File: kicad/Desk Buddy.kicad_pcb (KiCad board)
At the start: 2 copper layers, 62 parts, among them J1 USB_C_Receptacle_USB2.0_16P, J10 EXP_I2C1_2, J11 EXT_LED, J12 Conn_01x06, J13 Motor, J14 Conn_01x02, J15 TTP_1, J16 TTP_2, J17 UART, J2 LiPo, J3 GPIO48, J4 LCD_A, J5 LCD_B, J6 ToF, J7 AHT+BMP, J8 MPU6050, J9 EXP_I2C1_1, Q1 AO3400A, Q2 AO3400A, SW1 Push_EN, SW2 Push_BOOT, SW3 Switch_POWER, U1 USBLC6-2SC6, U2 BQ24075RGT, U3 AP2112K-3.3, U4 ESP32-S3-WROOM-1

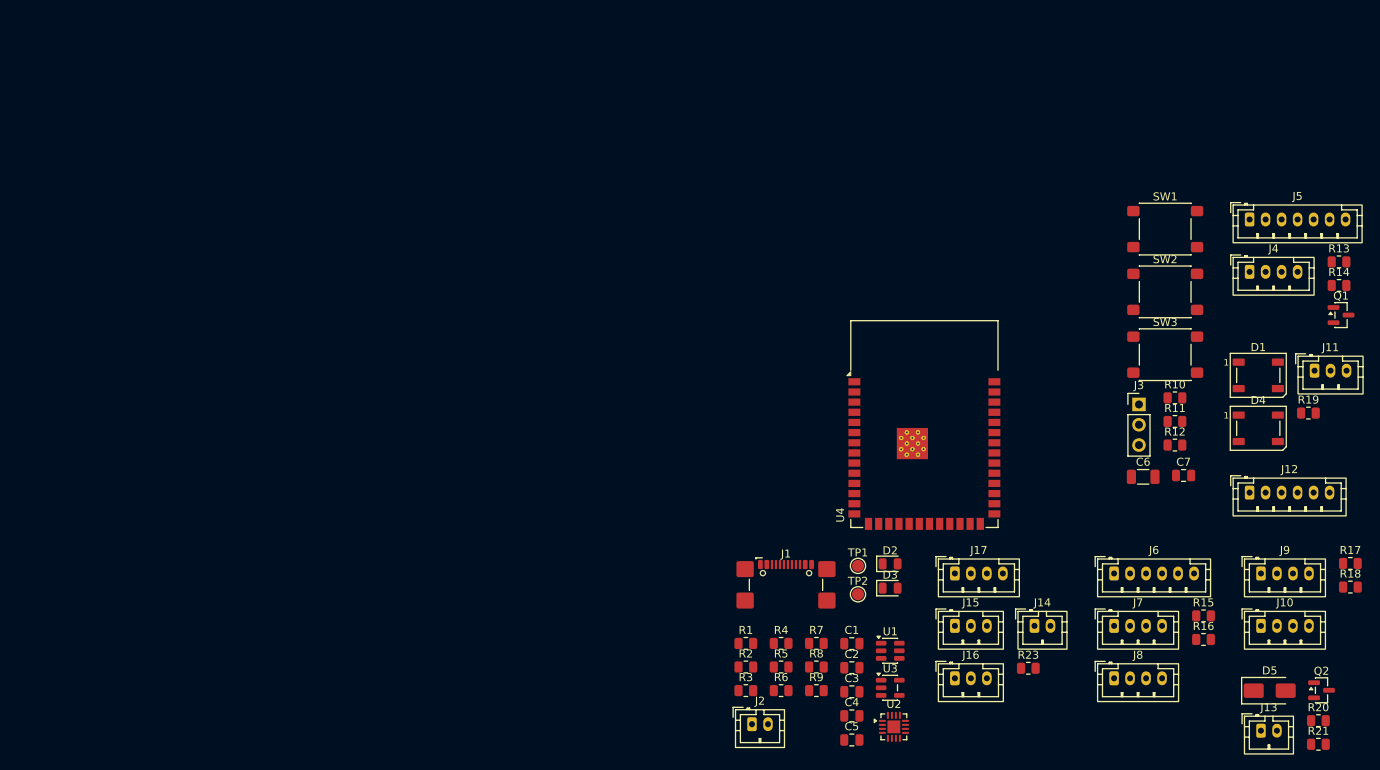
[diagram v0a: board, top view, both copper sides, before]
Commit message: PCB layout Adım 1: kart kurulumu
- Tasarım kuralları (0.2/0.2mm, via 0.8/0.4, kenar 0.3mm) ve net class'lar (Default/Power/Fine)
- Geçici outline 80x60mm, 3mm köşe yarıçapı
- 2x M3 delik (H1, H2) + 6mm bakır yasak alanlar
- ESP32 anten keepout rule-area (48x6.5mm, üst kenar)
- ESP32 termal via delikleri 0.2 -> 0.3mm

Co-Authored-By: Claude Sonnet 5.5 <noreply@anthropic.com>
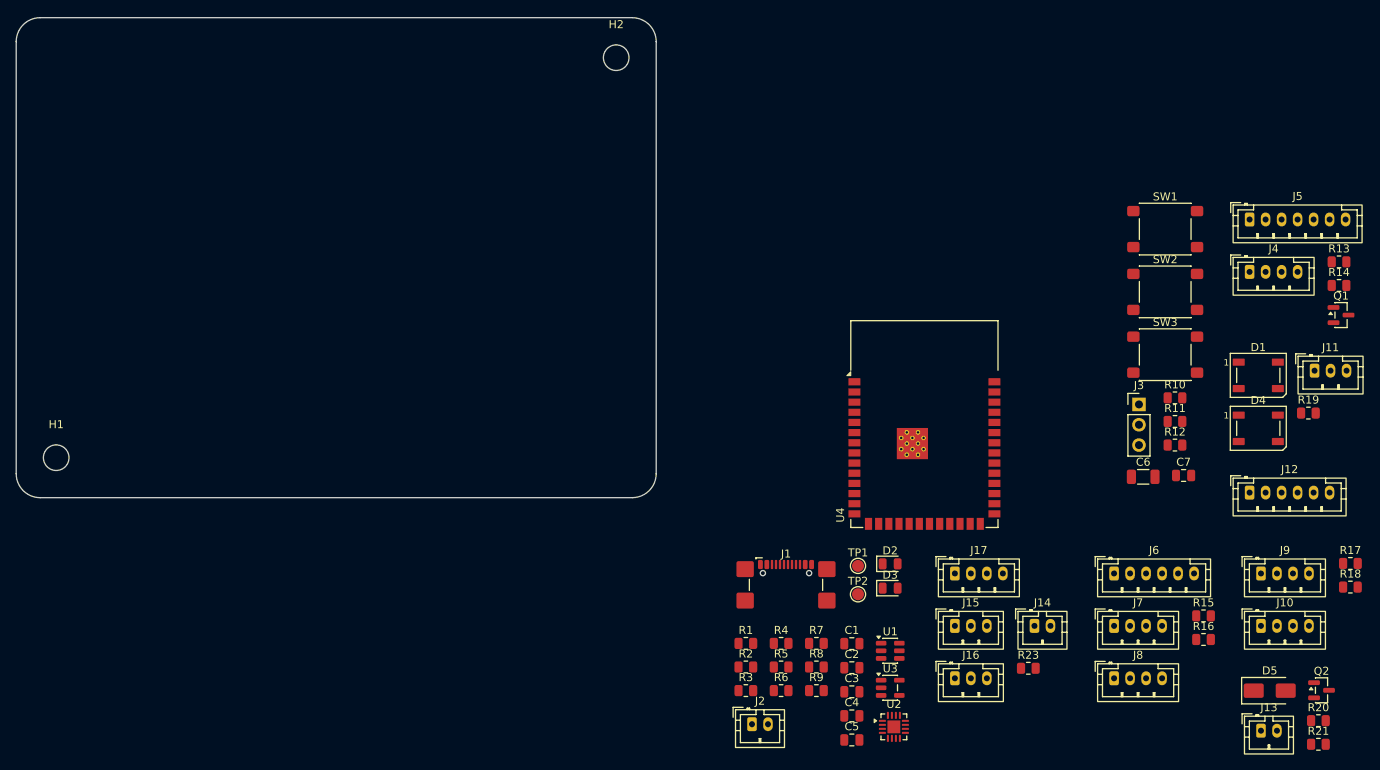
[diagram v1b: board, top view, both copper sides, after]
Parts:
- added H1: MountingHole_3.2mm_M3, MountingHole_3.2mm_M3, F.Cu at (25.0, 95.0)
- added H2: MountingHole_3.2mm_M3, MountingHole_3.2mm_M3, F.Cu at (95.0, 45.0)
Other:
- board outline added: 80 x 60 mm

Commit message: Şematik: I2C1_SCL IO45 yerine IO47'ye bağlandı
I2C1_SCL etiketi strapping pini IO45'e (pin 26) bağlıydı, notlardaki
atama GPIO47 (pin 24). Etiket pin 24'e, no_connect pin 26'ya taşındı.
PCB'de U4 net atamaları güncellendi, şematik parity 0 sorun.

Co-Authored-By: Claude Sonnet 5.5 <noreply@anthropic.com>
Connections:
- U4 pad 24: unconnected-(U4-IO47-Pad24) -> I2C1_SCL
- U4 pad 26: I2C1_SCL -> unconnected-(U4-IO45-Pad26)
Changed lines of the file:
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@@
 			(size 1.5 0.9)
 			(layers "F.Cu" "F.Mask" "F.Paste")
-			(net "unconnected-(U4-IO47-Pad24)")
+			(net "I2C1_SCL")
 			(pinfunction "IO47_24")
 			(pintype "bidirectional+no_connect")
@@
 			(size 1.5 0.9)
 			(layers "F.Cu" "F.Mask" "F.Paste")
-			(net "I2C1_SCL")
+			(net "unconnected-(U4-IO45-Pad26)")
 			(pinfunction "IO45_26")
 			(pintype "bidirectional")

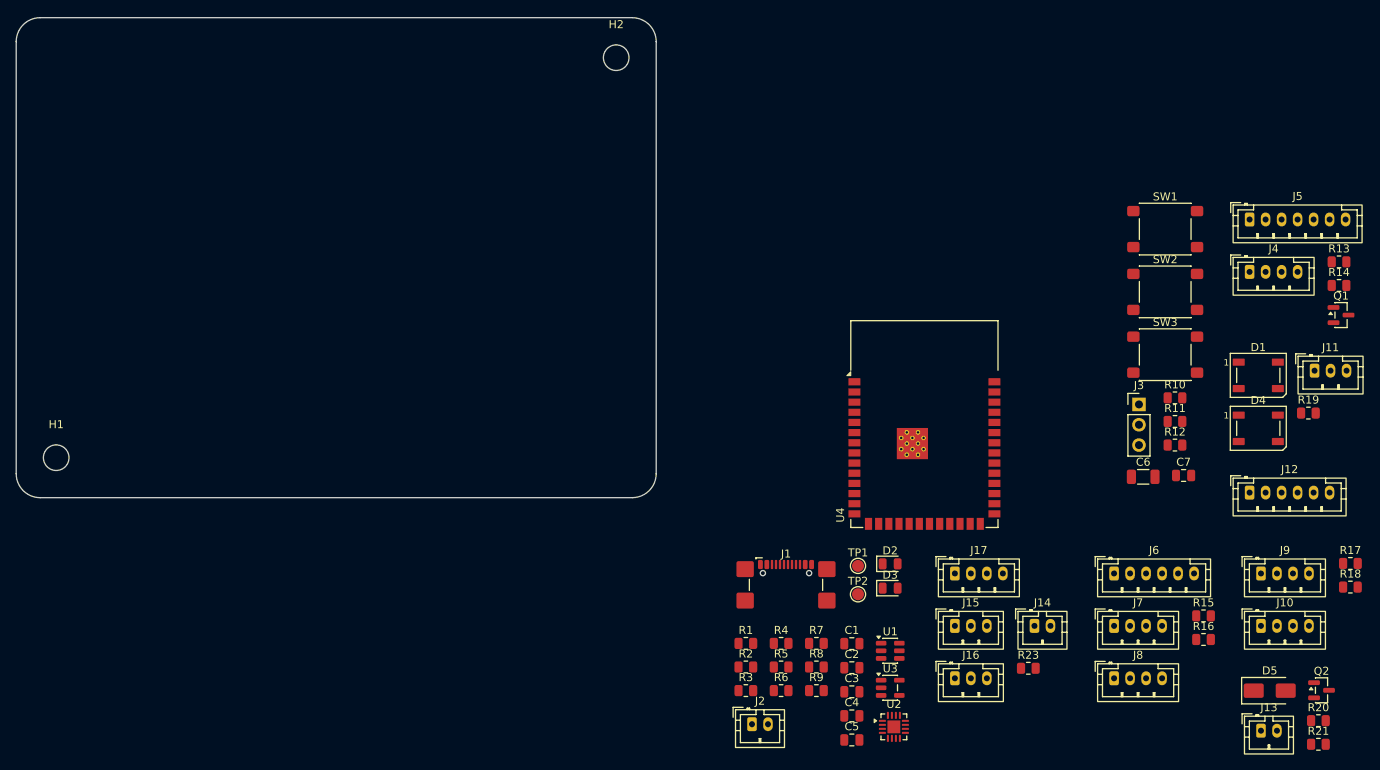
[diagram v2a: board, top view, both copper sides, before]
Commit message: PCB layout Adım 3a: güç bloğu yerleşimi
- Kart 90x65mm'ye büyütüldü, M3 delikleri ve anten keepout'u taşındı
- USB-C sol kenara hizalı, U1/U2/U3 ve bypass/ayar pasifleri pinlerine yakın yerleştirildi
- LiPo konnektörü, durum LED'leri, pil bölücü ve test noktaları yerleştirildi
- DRC: bakır/courtyard ihlali yok, şematik parity 0 sorun

Co-Authored-By: Claude Sonnet 5.5 <noreply@anthropic.com>
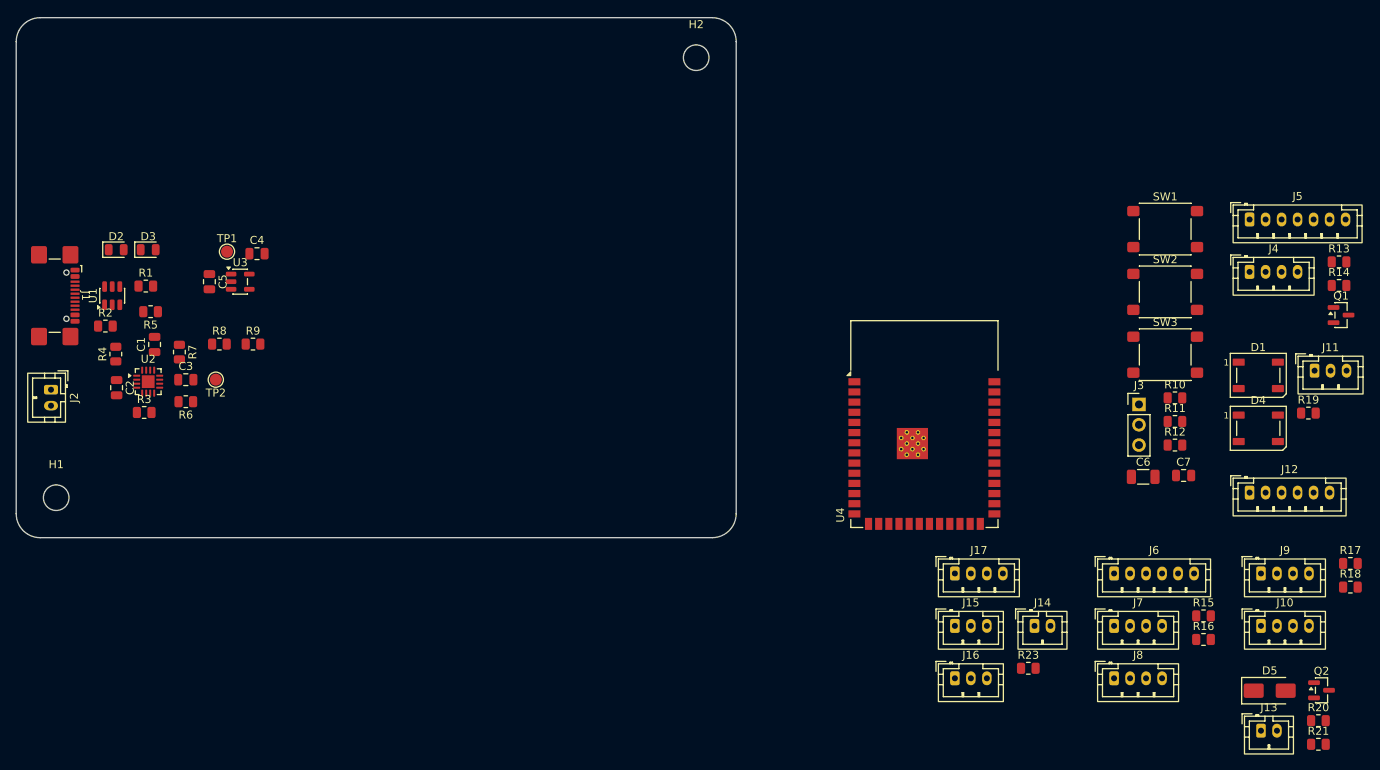
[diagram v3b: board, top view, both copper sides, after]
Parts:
- moved U1 106.9 mm to (32.0, 74.8), turned to 90 degrees
- moved D2 104.4 mm to (32.5, 69.0)
- moved U2 102.7 mm to (36.5, 85.5)
- moved D3 101.9 mm to (36.5, 69.0)
- moved J1 99.8 mm to (23.7, 74.8), turned to -90 degrees
- moved C5 98.6 mm to (44.1, 73.0), turned to -90 degrees
- moved C2 98.3 mm to (32.5, 86.2), turned to -90 degrees
- moved J2 97.1 mm to (24.4, 86.5), turned to -90 degrees
- moved U3 95.8 mm to (48.0, 73.0)
- moved C1 94.8 mm to (37.3, 80.8), turned to 90 degrees
- moved C4 94.2 mm to (50.1, 69.5)
- moved C3 91.9 mm to (41.2, 85.2)
- moved R2 90.7 mm to (31.1, 78.5)
- moved R4 90.7 mm to (32.5, 82.0), turned to 90 degrees
- moved R5 90.5 mm to (36.8, 76.8), turned to 180 degrees
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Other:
- board size 80 x 60 mm -> 90 x 65 mm

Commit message: PCB layout Adım 3b: MCU bloğu yerleşimi + harici güç butonu JST'si
- ESP32 anten ucu kart kenarına hizalı, C6/C7/R10, butonlar, pull-up'lar ve J3 yerleştirildi
- Şematik: GPIO2 için 3 pinli JST eklendi (J18 PWR_BTN: 3V3/GND/GPIO2), güç butonunun yanında
- Notlar: yumuşak kapatma güç tüketimi uyarısı, J18 kullanımı
- DRC: bakır/courtyard ihlali yok, şematik parity 0 sorun

Co-Authored-By: Claude Sonnet 5.5 <noreply@anthropic.com>
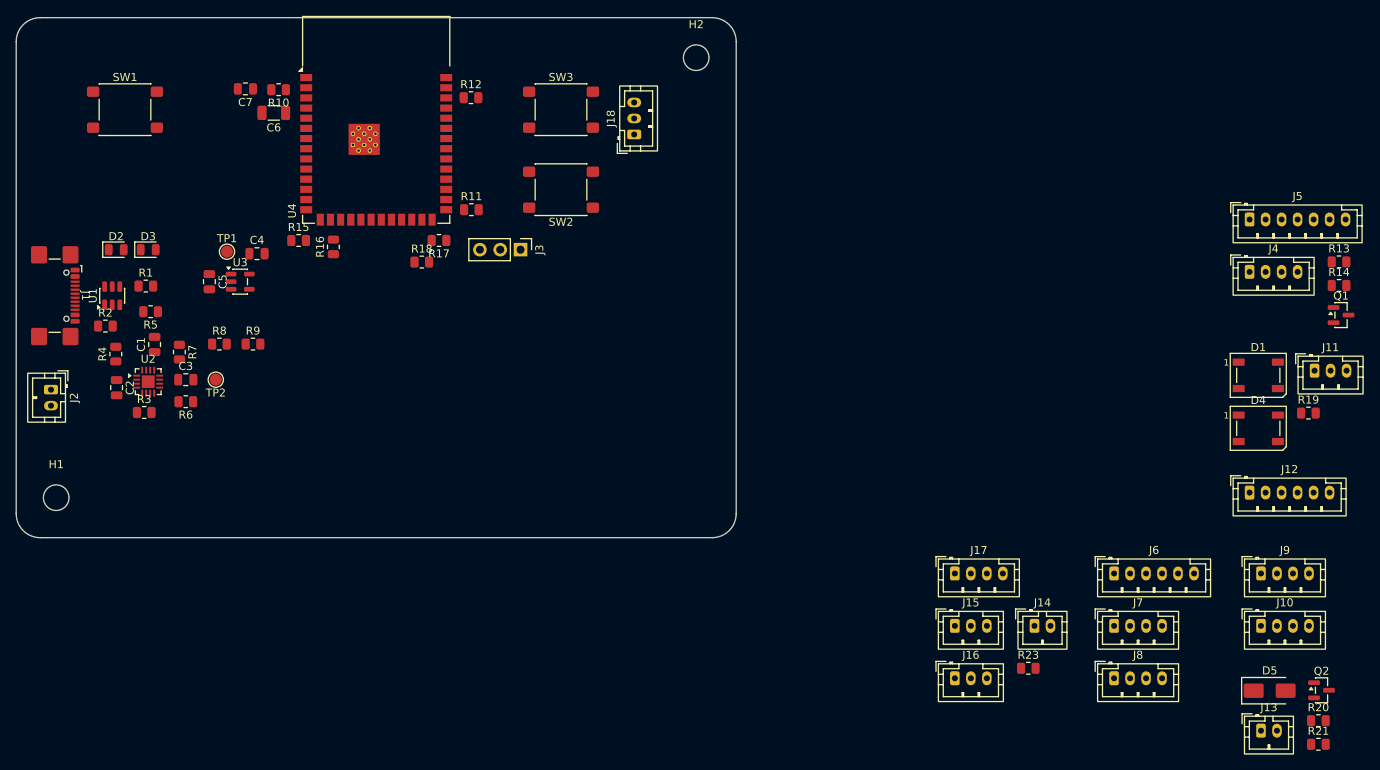
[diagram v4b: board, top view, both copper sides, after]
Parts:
- added J18: PWR_BTN, Connector_JST:JST_PH_B3B-PH-K_1x03_P2.00mm_Vertical, F.Cu at (97.2, 54.6)
- moved SW1 130.9 mm to (33.6, 51.5)
- moved C7 126.8 mm to (48.6, 48.9), turned to 180 degrees
- moved R18 123.0 mm to (70.7, 70.5)
- moved R15 122.5 mm to (55.3, 67.8)
- moved R17 120.9 mm to (72.8, 67.8), turned to 180 degrees
- moved R16 119.3 mm to (59.6, 68.7), turned to 90 degrees
- moved R10 118.5 mm to (52.8, 49.0), turned to 180 degrees
- moved C6 117.8 mm to (52.2, 51.9), turned to 180 degrees
- moved R12 98.1 mm to (76.8, 50.0)
- moved R11 91.8 mm to (76.9, 64.0)
- moved SW3 81.5 mm to (88.1, 51.5)
- moved J3 79.7 mm to (83.0, 69.0), turned to -90 degrees
- moved U4 78.4 mm to (65.0, 52.8)
- moved SW2 76.6 mm to (88.1, 61.5), turned to 180 degrees

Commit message: PCB layout Adım 3c (kısmen): çevre birimleri yerleşti, arka ışık devresi bekliyor
- Tüm JST konnektörleri, motor devresi, D1/D4, R19, R23 yerleştirildi
- Q1/R13/R14 yerleştirilmedi: LCD arka ışık devresi şematikte hatalı
  (Q1 drain'i VBAT_OUT'ta, LED pini de VBAT_OUT'ta; GPIO4 yüksekken pil rayı GND'ye kısa devre)
- Çözüm LCD modülündeki LED pininin türüne bağlı, ölçüm bekleniyor
- pcb-layout-plan.md eklendi: adım adım süreç, durum, açık sorun ve devam notları
- DRC: bakır/courtyard ihlali yok, şematik parity 0 sorun

Co-Authored-By: Claude Sonnet 5.5 <noreply@anthropic.com>
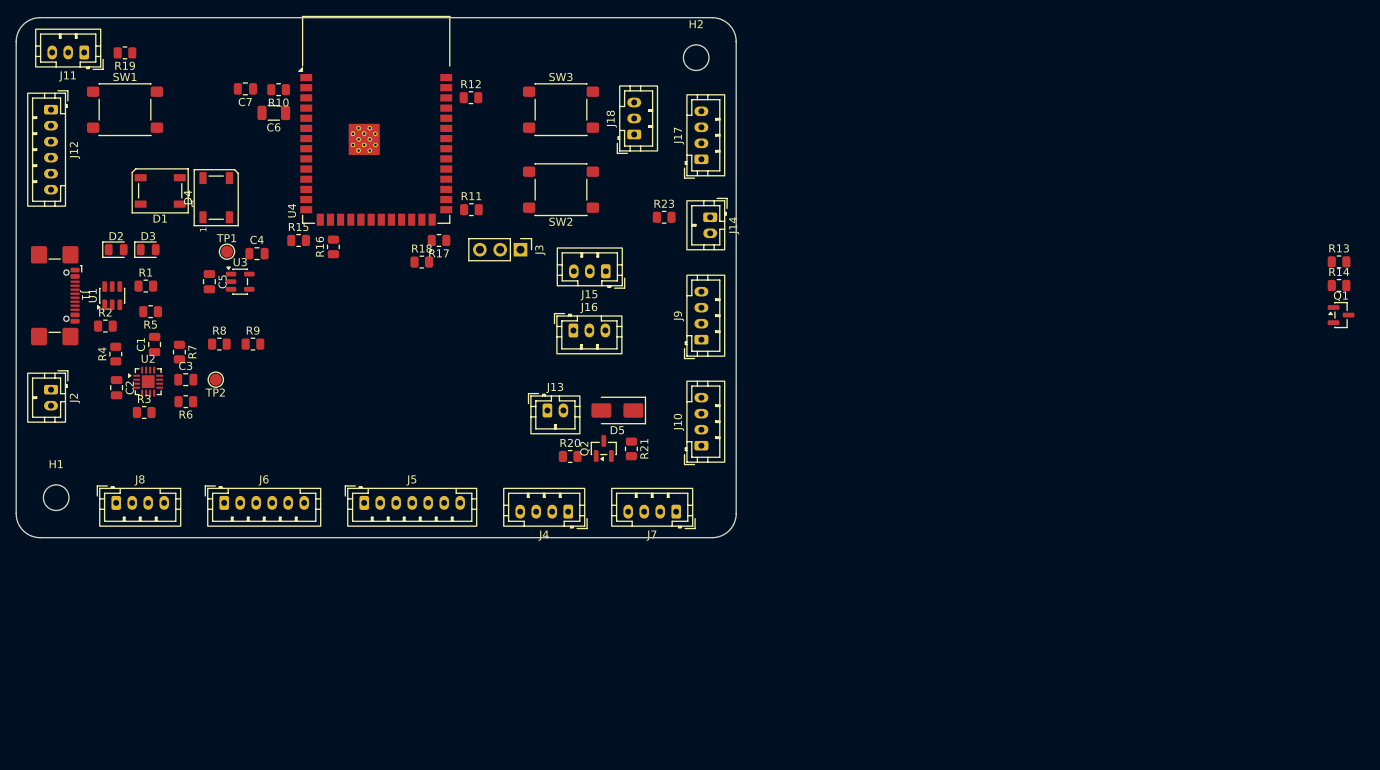
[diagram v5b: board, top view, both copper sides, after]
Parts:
- moved J11 158.9 mm to (28.5, 44.4), turned to 180 degrees
- moved J12 157.3 mm to (24.4, 51.5), turned to -90 degrees
- moved R19 154.6 mm to (33.6, 44.4), turned to 180 degrees
- moved D1 139.2 mm to (38.0, 61.6), turned to 180 degrees
- moved D4 133.4 mm to (45.0, 62.5), turned to 90 degrees
- moved J8 126.6 mm to (32.5, 100.7)
- moved J5 116.2 mm to (63.5, 100.7)
- moved J6 111.6 mm to (46.0, 100.7)
- moved R20 99.2 mm to (89.2, 94.8)
- moved J13 97.8 mm to (86.4, 89.1)
- moved Q2 94.7 mm to (93.5, 93.8), turned to 90 degrees
- moved R21 93.5 mm to (96.9, 93.9), turned to -90 degrees
- moved J4 90.3 mm to (89.0, 101.8), turned to 180 degrees
- moved D5 88.7 mm to (95.2, 89.1), turned to 180 degrees
- moved J9 75.8 mm to (105.7, 80.2), turned to 90 degrees
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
